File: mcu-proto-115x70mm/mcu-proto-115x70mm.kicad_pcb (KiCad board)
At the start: 2 copper layers, 115 x 70 mm, 1113 parts, among them J1 Conn_01x01

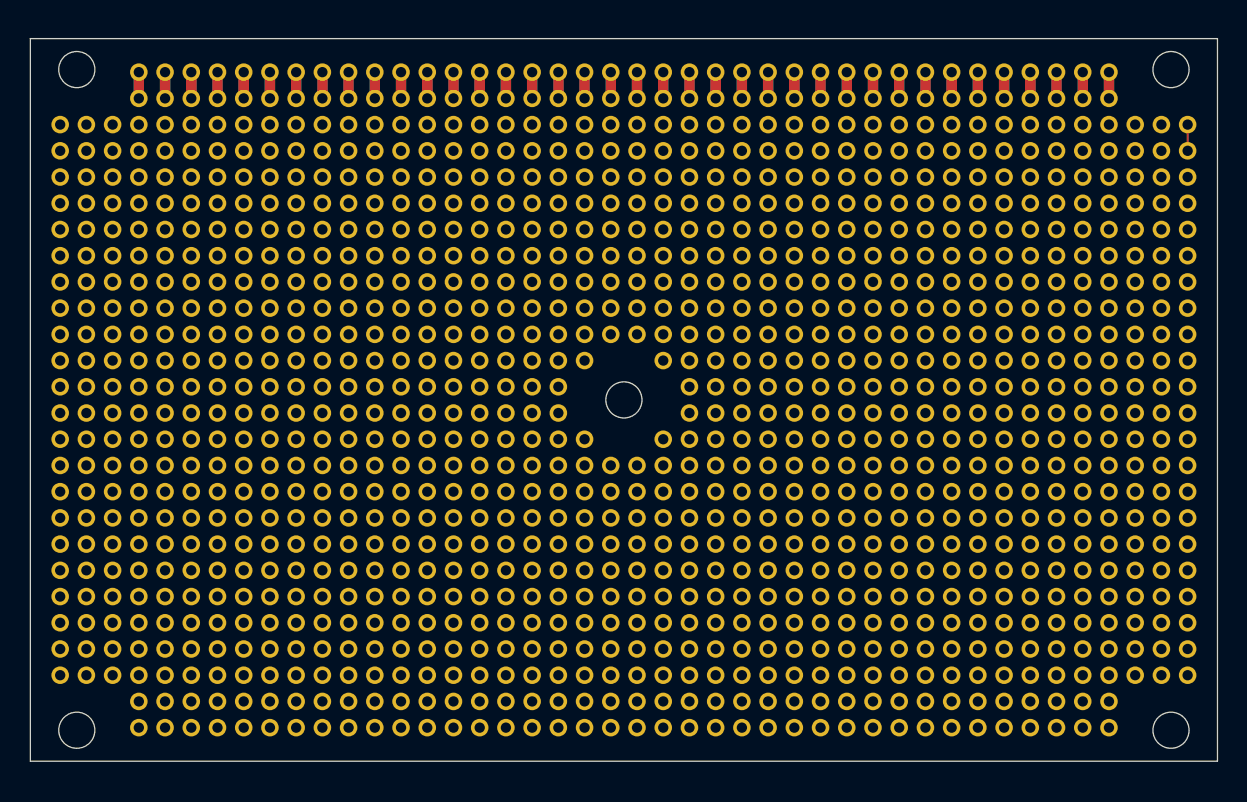
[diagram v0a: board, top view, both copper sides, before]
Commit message: Board routed with mounting holes and silkscreens ready
- Completed PCB routing for mcu-proto-115x70mm
- Added mounting holes for secure enclosure attachment
- Implemented silkscreen layer with component labels and markings
- Generated Gerber files and SVG previews for manufacturing
- Added PadLink footprint for enhanced connectivity
- Updated symbol library and footprint definitions
- Cleaned up old backup files and added new development snapshots
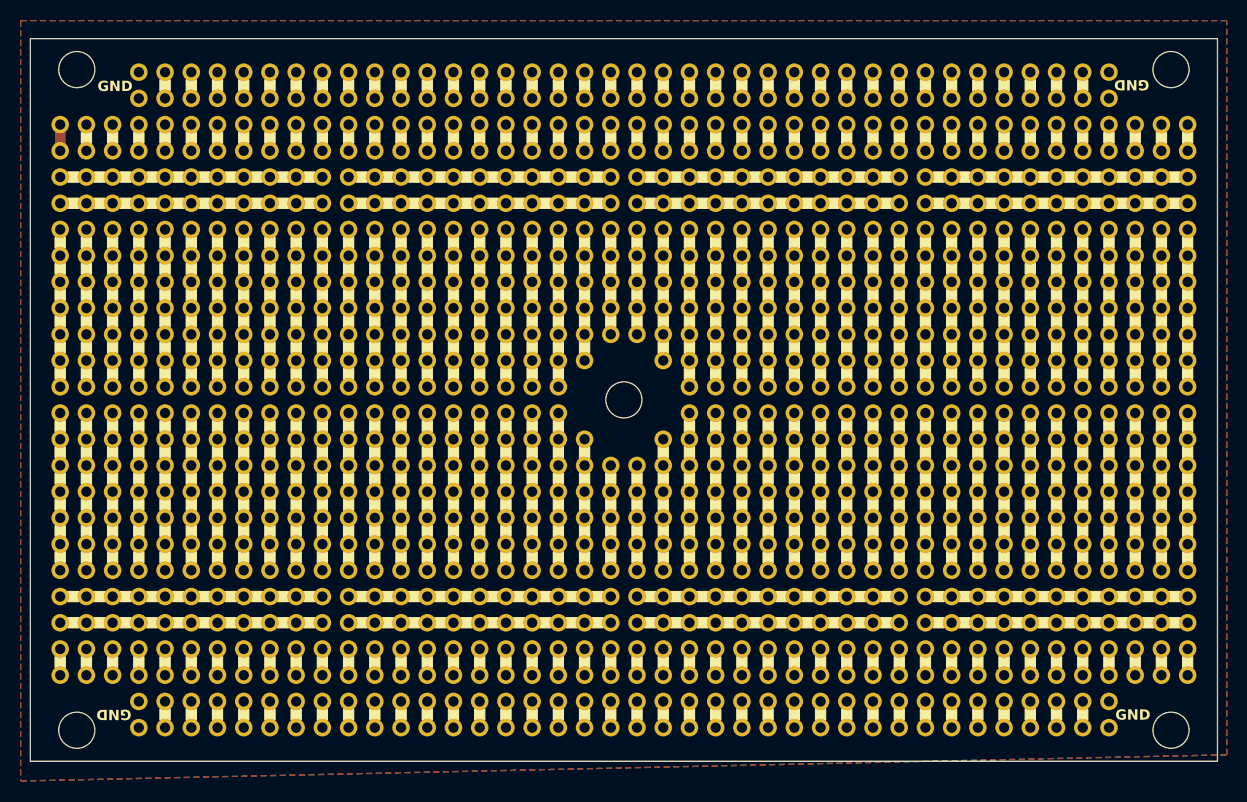
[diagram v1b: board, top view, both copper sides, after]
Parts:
- removed J1 (x1108): Conn_01x01, proto-pcb-pads:RoundPad_1.7mm_Hole_1.0mm
- added REF**: Round_Pad_1.7mm_Hole_1.0mm, proto-pcb-pads:RoundPad_1.7mm_Hole_1.0mm, F.Cu at (110.5, 53.2)
- added REF**: Pad_Link_1.7mm_Width_1.0mm, proto-pcb-silks:PadLink_1.7mm_Width_1.0mm, F.Cu at (113.0, 53.2)
- added REF**: Round_Pad_1.7mm_Hole_1.0mm, proto-pcb-pads:RoundPad_1.7mm_Hole_1.0mm, F.Cu at (113.0, 53.2)
- added REF**1: Round_Pad_1.7mm_Hole_1.0mm, proto-pcb-pads:RoundPad_1.7mm_Hole_1.0mm, F.Cu at (115.6, 53.2)
- added REF**10: Round_Pad_1.7mm_Hole_1.0mm, proto-pcb-pads:RoundPad_1.7mm_Hole_1.0mm, F.Cu at (138.4, 53.2)
- added REF**100: Round_Pad_1.7mm_Hole_1.0mm, proto-pcb-pads:RoundPad_1.7mm_Hole_1.0mm, F.Cu at (163.8, 58.3)
- added REF**1000: Round_Pad_1.7mm_Hole_1.0mm, proto-pcb-pads:RoundPad_1.7mm_Hole_1.0mm, F.Cu at (102.9, 111.7)
- added REF**1001: Round_Pad_1.7mm_Hole_1.0mm, proto-pcb-pads:RoundPad_1.7mm_Hole_1.0mm, F.Cu at (105.4, 111.7)
- added REF**1002: Round_Pad_1.7mm_Hole_1.0mm, proto-pcb-pads:RoundPad_1.7mm_Hole_1.0mm, F.Cu at (108.0, 111.7)
- added REF**1003: Round_Pad_1.7mm_Hole_1.0mm, proto-pcb-pads:RoundPad_1.7mm_Hole_1.0mm, F.Cu at (110.5, 111.7)
- added REF**1004: Round_Pad_1.7mm_Hole_1.0mm, proto-pcb-pads:RoundPad_1.7mm_Hole_1.0mm, F.Cu at (113.0, 111.7)
- added REF**1005: Round_Pad_1.7mm_Hole_1.0mm, proto-pcb-pads:RoundPad_1.7mm_Hole_1.0mm, F.Cu at (115.6, 111.7)
- added REF**1006: Round_Pad_1.7mm_Hole_1.0mm, proto-pcb-pads:RoundPad_1.7mm_Hole_1.0mm, F.Cu at (118.1, 111.7)
- added REF**1007: Round_Pad_1.7mm_Hole_1.0mm, proto-pcb-pads:RoundPad_1.7mm_Hole_1.0mm, F.Cu at (120.7, 111.7)
- added REF**1008: Round_Pad_1.7mm_Hole_1.0mm, proto-pcb-pads:RoundPad_1.7mm_Hole_1.0mm, F.Cu at (123.2, 111.7)
- added REF**1009: Round_Pad_1.7mm_Hole_1.0mm, proto-pcb-pads:RoundPad_1.7mm_Hole_1.0mm, F.Cu at (125.8, 111.7)
- added REF**101: Round_Pad_1.7mm_Hole_1.0mm, proto-pcb-pads:RoundPad_1.7mm_Hole_1.0mm, F.Cu at (166.4, 58.3)
- added REF**1010: Round_Pad_1.7mm_Hole_1.0mm, proto-pcb-pads:RoundPad_1.7mm_Hole_1.0mm, F.Cu at (128.3, 111.7)
- added REF**1011: Round_Pad_1.7mm_Hole_1.0mm, proto-pcb-pads:RoundPad_1.7mm_Hole_1.0mm, F.Cu at (130.8, 111.7)
- added REF**1012: Round_Pad_1.7mm_Hole_1.0mm, proto-pcb-pads:RoundPad_1.7mm_Hole_1.0mm, F.Cu at (133.4, 111.7)
- added REF**1013: Round_Pad_1.7mm_Hole_1.0mm, proto-pcb-pads:RoundPad_1.7mm_Hole_1.0mm, F.Cu at (135.9, 111.7)
- added REF**1014: Round_Pad_1.7mm_Hole_1.0mm, proto-pcb-pads:RoundPad_1.7mm_Hole_1.0mm, F.Cu at (138.4, 111.7)
- added REF**1015: Round_Pad_1.7mm_Hole_1.0mm, proto-pcb-pads:RoundPad_1.7mm_Hole_1.0mm, F.Cu at (141.0, 111.7)
- added REF**1016: Round_Pad_1.7mm_Hole_1.0mm, proto-pcb-pads:RoundPad_1.7mm_Hole_1.0mm, F.Cu at (143.5, 111.7)
- added REF**1017: Round_Pad_1.7mm_Hole_1.0mm, proto-pcb-pads:RoundPad_1.7mm_Hole_1.0mm, F.Cu at (146.1, 111.7)
- added REF**1018: Round_Pad_1.7mm_Hole_1.0mm, proto-pcb-pads:RoundPad_1.7mm_Hole_1.0mm, F.Cu at (148.6, 111.7)
- added REF**1019: Round_Pad_1.7mm_Hole_1.0mm, proto-pcb-pads:RoundPad_1.7mm_Hole_1.0mm, F.Cu at (151.2, 111.7)
- added REF**102: Round_Pad_1.7mm_Hole_1.0mm, proto-pcb-pads:RoundPad_1.7mm_Hole_1.0mm, F.Cu at (168.9, 58.3)
- added REF**1020: Round_Pad_1.7mm_Hole_1.0mm, proto-pcb-pads:RoundPad_1.7mm_Hole_1.0mm, F.Cu at (153.7, 111.7)
- added REF**1021: Round_Pad_1.7mm_Hole_1.0mm, proto-pcb-pads:RoundPad_1.7mm_Hole_1.0mm, F.Cu at (156.2, 111.7)
- added REF**1022: Round_Pad_1.7mm_Hole_1.0mm, proto-pcb-pads:RoundPad_1.7mm_Hole_1.0mm, F.Cu at (158.8, 111.7)
- added REF**1023: Round_Pad_1.7mm_Hole_1.0mm, proto-pcb-pads:RoundPad_1.7mm_Hole_1.0mm, F.Cu at (161.3, 111.7)
- added REF**1024: Round_Pad_1.7mm_Hole_1.0mm, proto-pcb-pads:RoundPad_1.7mm_Hole_1.0mm, F.Cu at (163.8, 111.7)
- added REF**1025: Round_Pad_1.7mm_Hole_1.0mm, proto-pcb-pads:RoundPad_1.7mm_Hole_1.0mm, F.Cu at (166.4, 111.7)
- added REF**1026: Round_Pad_1.7mm_Hole_1.0mm, proto-pcb-pads:RoundPad_1.7mm_Hole_1.0mm, F.Cu at (168.9, 111.7)
- added REF**1027: Round_Pad_1.7mm_Hole_1.0mm, proto-pcb-pads:RoundPad_1.7mm_Hole_1.0mm, F.Cu at (171.5, 111.7)
- added REF**1028: Round_Pad_1.7mm_Hole_1.0mm, proto-pcb-pads:RoundPad_1.7mm_Hole_1.0mm, F.Cu at (174.0, 111.7)
- added REF**1029: Round_Pad_1.7mm_Hole_1.0mm, proto-pcb-pads:RoundPad_1.7mm_Hole_1.0mm, F.Cu at (176.6, 111.7)
- added REF**103: Round_Pad_1.7mm_Hole_1.0mm, proto-pcb-pads:RoundPad_1.7mm_Hole_1.0mm, F.Cu at (171.5, 58.3)
- added REF**1030: Round_Pad_1.7mm_Hole_1.0mm, proto-pcb-pads:RoundPad_1.7mm_Hole_1.0mm, F.Cu at (179.1, 111.7)
- added REF**1031: Round_Pad_1.7mm_Hole_1.0mm, proto-pcb-pads:RoundPad_1.7mm_Hole_1.0mm, F.Cu at (181.6, 111.7)
- added REF**1032: Round_Pad_1.7mm_Hole_1.0mm, proto-pcb-pads:RoundPad_1.7mm_Hole_1.0mm, F.Cu at (184.2, 111.7)
- added REF**1033: Round_Pad_1.7mm_Hole_1.0mm, proto-pcb-pads:RoundPad_1.7mm_Hole_1.0mm, F.Cu at (186.7, 111.7)
- added REF**1034: Round_Pad_1.7mm_Hole_1.0mm, proto-pcb-pads:RoundPad_1.7mm_Hole_1.0mm, F.Cu at (189.2, 111.7)
- added REF**1035: Round_Pad_1.7mm_Hole_1.0mm, proto-pcb-pads:RoundPad_1.7mm_Hole_1.0mm, F.Cu at (191.8, 111.7)
- added REF**1036: Round_Pad_1.7mm_Hole_1.0mm, proto-pcb-pads:RoundPad_1.7mm_Hole_1.0mm, F.Cu at (194.3, 111.7)
- added REF**1037: Round_Pad_1.7mm_Hole_1.0mm, proto-pcb-pads:RoundPad_1.7mm_Hole_1.0mm, F.Cu at (196.9, 111.7)
- added REF**1038: Round_Pad_1.7mm_Hole_1.0mm, proto-pcb-pads:RoundPad_1.7mm_Hole_1.0mm, F.Cu at (199.4, 111.7)
- added REF**1039: Round_Pad_1.7mm_Hole_1.0mm, proto-pcb-pads:RoundPad_1.7mm_Hole_1.0mm, F.Cu at (201.9, 111.7)
- added REF**104: Round_Pad_1.7mm_Hole_1.0mm, proto-pcb-pads:RoundPad_1.7mm_Hole_1.0mm, F.Cu at (174.0, 58.3)
- added REF**1040: Round_Pad_1.7mm_Hole_1.0mm, proto-pcb-pads:RoundPad_1.7mm_Hole_1.0mm, F.Cu at (204.5, 111.7)
- added REF**1041: Round_Pad_1.7mm_Hole_1.0mm, proto-pcb-pads:RoundPad_1.7mm_Hole_1.0mm, F.Cu at (207.0, 111.7)
- added REF**1042: Round_Pad_1.7mm_Hole_1.0mm, proto-pcb-pads:RoundPad_1.7mm_Hole_1.0mm, F.Cu at (209.6, 111.7)
- added REF**1043: Round_Pad_1.7mm_Hole_1.0mm, proto-pcb-pads:RoundPad_1.7mm_Hole_1.0mm, F.Cu at (212.1, 111.7)
- added REF**1044: Pad_Link_1.7mm_Width_1.0mm, proto-pcb-silks:PadLink_1.7mm_Width_1.0mm, F.Cu at (148.6, 53.2)
- added REF**1045: Pad_Link_1.7mm_Width_1.0mm, proto-pcb-silks:PadLink_1.7mm_Width_1.0mm, F.Cu at (151.2, 53.2)
- added REF**1046: Pad_Link_1.7mm_Width_1.0mm, proto-pcb-silks:PadLink_1.7mm_Width_1.0mm, F.Cu at (153.7, 53.2)
- added REF**1047: Round_Pad_1.7mm_Hole_1.0mm, proto-pcb-pads:RoundPad_1.7mm_Hole_1.0mm, F.Cu at (110.5, 114.2)
- added REF**1048: Round_Pad_1.7mm_Hole_1.0mm, proto-pcb-pads:RoundPad_1.7mm_Hole_1.0mm, F.Cu at (113.0, 114.2)
- added REF**1049: Round_Pad_1.7mm_Hole_1.0mm, proto-pcb-pads:RoundPad_1.7mm_Hole_1.0mm, F.Cu at (115.6, 114.2)
- added REF**105: Round_Pad_1.7mm_Hole_1.0mm, proto-pcb-pads:RoundPad_1.7mm_Hole_1.0mm, F.Cu at (176.6, 58.3)
- added REF**1050: Round_Pad_1.7mm_Hole_1.0mm, proto-pcb-pads:RoundPad_1.7mm_Hole_1.0mm, F.Cu at (118.1, 114.2)
- added REF**1051: Round_Pad_1.7mm_Hole_1.0mm, proto-pcb-pads:RoundPad_1.7mm_Hole_1.0mm, F.Cu at (120.7, 114.2)
- added REF**1052: Round_Pad_1.7mm_Hole_1.0mm, proto-pcb-pads:RoundPad_1.7mm_Hole_1.0mm, F.Cu at (123.2, 114.2)
- added REF**1053: Round_Pad_1.7mm_Hole_1.0mm, proto-pcb-pads:RoundPad_1.7mm_Hole_1.0mm, F.Cu at (125.8, 114.2)
- added REF**1054: Round_Pad_1.7mm_Hole_1.0mm, proto-pcb-pads:RoundPad_1.7mm_Hole_1.0mm, F.Cu at (128.3, 114.2)
- added REF**1055: Round_Pad_1.7mm_Hole_1.0mm, proto-pcb-pads:RoundPad_1.7mm_Hole_1.0mm, F.Cu at (130.8, 114.2)
- added REF**1056: Round_Pad_1.7mm_Hole_1.0mm, proto-pcb-pads:RoundPad_1.7mm_Hole_1.0mm, F.Cu at (133.4, 114.2)
- added REF**1057: Round_Pad_1.7mm_Hole_1.0mm, proto-pcb-pads:RoundPad_1.7mm_Hole_1.0mm, F.Cu at (135.9, 114.2)
- added REF**1058: Round_Pad_1.7mm_Hole_1.0mm, proto-pcb-pads:RoundPad_1.7mm_Hole_1.0mm, F.Cu at (138.4, 114.2)
- added REF**1059: Round_Pad_1.7mm_Hole_1.0mm, proto-pcb-pads:RoundPad_1.7mm_Hole_1.0mm, F.Cu at (141.0, 114.2)
- added REF**106: Round_Pad_1.7mm_Hole_1.0mm, proto-pcb-pads:RoundPad_1.7mm_Hole_1.0mm, F.Cu at (179.1, 58.3)
- added REF**1060: Round_Pad_1.7mm_Hole_1.0mm, proto-pcb-pads:RoundPad_1.7mm_Hole_1.0mm, F.Cu at (143.5, 114.2)
- added REF**1061: Round_Pad_1.7mm_Hole_1.0mm, proto-pcb-pads:RoundPad_1.7mm_Hole_1.0mm, F.Cu at (146.1, 114.2)
- added REF**1062: Round_Pad_1.7mm_Hole_1.0mm, proto-pcb-pads:RoundPad_1.7mm_Hole_1.0mm, F.Cu at (148.6, 114.2)
- added REF**1063: Round_Pad_1.7mm_Hole_1.0mm, proto-pcb-pads:RoundPad_1.7mm_Hole_1.0mm, F.Cu at (151.2, 114.2)
- added REF**1064: Round_Pad_1.7mm_Hole_1.0mm, proto-pcb-pads:RoundPad_1.7mm_Hole_1.0mm, F.Cu at (153.7, 114.2)
- added REF**1065: Round_Pad_1.7mm_Hole_1.0mm, proto-pcb-pads:RoundPad_1.7mm_Hole_1.0mm, F.Cu at (156.2, 114.2)
- added REF**1066: Round_Pad_1.7mm_Hole_1.0mm, proto-pcb-pads:RoundPad_1.7mm_Hole_1.0mm, F.Cu at (158.8, 114.2)
- added REF**1067: Round_Pad_1.7mm_Hole_1.0mm, proto-pcb-pads:RoundPad_1.7mm_Hole_1.0mm, F.Cu at (161.3, 114.2)
- added REF**1068: Round_Pad_1.7mm_Hole_1.0mm, proto-pcb-pads:RoundPad_1.7mm_Hole_1.0mm, F.Cu at (163.8, 114.2)
- added REF**1069: Round_Pad_1.7mm_Hole_1.0mm, proto-pcb-pads:RoundPad_1.7mm_Hole_1.0mm, F.Cu at (166.4, 114.2)
- added REF**107: Round_Pad_1.7mm_Hole_1.0mm, proto-pcb-pads:RoundPad_1.7mm_Hole_1.0mm, F.Cu at (181.6, 58.3)
- added REF**1070: Round_Pad_1.7mm_Hole_1.0mm, proto-pcb-pads:RoundPad_1.7mm_Hole_1.0mm, F.Cu at (168.9, 114.2)
- added REF**1071: Round_Pad_1.7mm_Hole_1.0mm, proto-pcb-pads:RoundPad_1.7mm_Hole_1.0mm, F.Cu at (171.5, 114.2)
- added REF**1072: Round_Pad_1.7mm_Hole_1.0mm, proto-pcb-pads:RoundPad_1.7mm_Hole_1.0mm, F.Cu at (174.0, 114.2)
- added REF**1073: Round_Pad_1.7mm_Hole_1.0mm, proto-pcb-pads:RoundPad_1.7mm_Hole_1.0mm, F.Cu at (176.6, 114.2)
- added REF**1074: Round_Pad_1.7mm_Hole_1.0mm, proto-pcb-pads:RoundPad_1.7mm_Hole_1.0mm, F.Cu at (179.1, 114.2)
- added REF**1075: Round_Pad_1.7mm_Hole_1.0mm, proto-pcb-pads:RoundPad_1.7mm_Hole_1.0mm, F.Cu at (181.6, 114.2)
- added REF**1076: Round_Pad_1.7mm_Hole_1.0mm, proto-pcb-pads:RoundPad_1.7mm_Hole_1.0mm, F.Cu at (184.2, 114.2)
- added REF**1077: Round_Pad_1.7mm_Hole_1.0mm, proto-pcb-pads:RoundPad_1.7mm_Hole_1.0mm, F.Cu at (186.7, 114.2)
- added REF**1078: Round_Pad_1.7mm_Hole_1.0mm, proto-pcb-pads:RoundPad_1.7mm_Hole_1.0mm, F.Cu at (189.2, 114.2)
- added REF**1079: Round_Pad_1.7mm_Hole_1.0mm, proto-pcb-pads:RoundPad_1.7mm_Hole_1.0mm, F.Cu at (191.8, 114.2)
- added REF**108: Round_Pad_1.7mm_Hole_1.0mm, proto-pcb-pads:RoundPad_1.7mm_Hole_1.0mm, F.Cu at (184.2, 58.3)
- added REF**1080: Round_Pad_1.7mm_Hole_1.0mm, proto-pcb-pads:RoundPad_1.7mm_Hole_1.0mm, F.Cu at (194.3, 114.2)
- added REF**1081: Round_Pad_1.7mm_Hole_1.0mm, proto-pcb-pads:RoundPad_1.7mm_Hole_1.0mm, F.Cu at (196.9, 114.2)
- added REF**1082: Round_Pad_1.7mm_Hole_1.0mm, proto-pcb-pads:RoundPad_1.7mm_Hole_1.0mm, F.Cu at (199.4, 114.2)
- added REF**1083: Round_Pad_1.7mm_Hole_1.0mm, proto-pcb-pads:RoundPad_1.7mm_Hole_1.0mm, F.Cu at (201.9, 114.2)
- added REF**1084: Round_Pad_1.7mm_Hole_1.0mm, proto-pcb-pads:RoundPad_1.7mm_Hole_1.0mm, F.Cu at (204.5, 114.2)
- added REF**1085: Pad_Link_1.7mm_Width_1.0mm, proto-pcb-silks:PadLink_1.7mm_Width_1.0mm, F.Cu at (156.2, 53.2)
- added REF**1086: Pad_Link_1.7mm_Width_1.0mm, proto-pcb-silks:PadLink_1.7mm_Width_1.0mm, F.Cu at (158.8, 53.2)
- added REF**1087: Pad_Link_1.7mm_Width_1.0mm, proto-pcb-silks:PadLink_1.7mm_Width_1.0mm, F.Cu at (161.3, 53.2)
- added REF**1088: Pad_Link_1.7mm_Width_1.0mm, proto-pcb-silks:PadLink_1.7mm_Width_1.0mm, F.Cu at (163.8, 53.2)
- added REF**1089: Pad_Link_1.7mm_Width_1.0mm, proto-pcb-silks:PadLink_1.7mm_Width_1.0mm, F.Cu at (166.4, 53.2)
- added REF**109: Round_Pad_1.7mm_Hole_1.0mm, proto-pcb-pads:RoundPad_1.7mm_Hole_1.0mm, F.Cu at (186.7, 58.3)
- added REF**1090: Pad_Link_1.7mm_Width_1.0mm, proto-pcb-silks:PadLink_1.7mm_Width_1.0mm, F.Cu at (168.9, 53.2)
- added REF**1091: Round_Pad_1.7mm_Hole_1.0mm, proto-pcb-pads:RoundPad_1.7mm_Hole_1.0mm, F.Cu at (110.5, 116.8)
- added REF**1092: Round_Pad_1.7mm_Hole_1.0mm, proto-pcb-pads:RoundPad_1.7mm_Hole_1.0mm, F.Cu at (113.0, 116.8)
- added REF**1093: Round_Pad_1.7mm_Hole_1.0mm, proto-pcb-pads:RoundPad_1.7mm_Hole_1.0mm, F.Cu at (115.6, 116.8)
- added REF**1094: Round_Pad_1.7mm_Hole_1.0mm, proto-pcb-pads:RoundPad_1.7mm_Hole_1.0mm, F.Cu at (118.1, 116.8)
- added REF**1095: Round_Pad_1.7mm_Hole_1.0mm, proto-pcb-pads:RoundPad_1.7mm_Hole_1.0mm, F.Cu at (120.7, 116.8)
- added REF**1096: Round_Pad_1.7mm_Hole_1.0mm, proto-pcb-pads:RoundPad_1.7mm_Hole_1.0mm, F.Cu at (123.2, 116.8)
- added REF**1097: Round_Pad_1.7mm_Hole_1.0mm, proto-pcb-pads:RoundPad_1.7mm_Hole_1.0mm, F.Cu at (125.8, 116.8)
- added REF**1098: Round_Pad_1.7mm_Hole_1.0mm, proto-pcb-pads:RoundPad_1.7mm_Hole_1.0mm, F.Cu at (128.3, 116.8)
- added REF**1099: Round_Pad_1.7mm_Hole_1.0mm, proto-pcb-pads:RoundPad_1.7mm_Hole_1.0mm, F.Cu at (130.8, 116.8)
- added REF**11: Round_Pad_1.7mm_Hole_1.0mm, proto-pcb-pads:RoundPad_1.7mm_Hole_1.0mm, F.Cu at (141.0, 53.2)
- added REF**110: Round_Pad_1.7mm_Hole_1.0mm, proto-pcb-pads:RoundPad_1.7mm_Hole_1.0mm, F.Cu at (189.2, 58.3)
- added REF**1100: Round_Pad_1.7mm_Hole_1.0mm, proto-pcb-pads:RoundPad_1.7mm_Hole_1.0mm, F.Cu at (133.4, 116.8)
- added REF**1101: Round_Pad_1.7mm_Hole_1.0mm, proto-pcb-pads:RoundPad_1.7mm_Hole_1.0mm, F.Cu at (135.9, 116.8)
- added REF**1102: Round_Pad_1.7mm_Hole_1.0mm, proto-pcb-pads:RoundPad_1.7mm_Hole_1.0mm, F.Cu at (138.4, 116.8)
- added REF**1103: Round_Pad_1.7mm_Hole_1.0mm, proto-pcb-pads:RoundPad_1.7mm_Hole_1.0mm, F.Cu at (141.0, 116.8)
- added REF**1104: Round_Pad_1.7mm_Hole_1.0mm, proto-pcb-pads:RoundPad_1.7mm_Hole_1.0mm, F.Cu at (143.5, 116.8)
- added REF**1105: Round_Pad_1.7mm_Hole_1.0mm, proto-pcb-pads:RoundPad_1.7mm_Hole_1.0mm, F.Cu at (146.1, 116.8)
- added REF**1106: Round_Pad_1.7mm_Hole_1.0mm, proto-pcb-pads:RoundPad_1.7mm_Hole_1.0mm, F.Cu at (148.6, 116.8)
- added REF**1107: Round_Pad_1.7mm_Hole_1.0mm, proto-pcb-pads:RoundPad_1.7mm_Hole_1.0mm, F.Cu at (151.2, 116.8)
- added REF**1108: Round_Pad_1.7mm_Hole_1.0mm, proto-pcb-pads:RoundPad_1.7mm_Hole_1.0mm, F.Cu at (153.7, 116.8)
- added REF**1109: Round_Pad_1.7mm_Hole_1.0mm, proto-pcb-pads:RoundPad_1.7mm_Hole_1.0mm, F.Cu at (156.2, 116.8)
- added REF**111: Round_Pad_1.7mm_Hole_1.0mm, proto-pcb-pads:RoundPad_1.7mm_Hole_1.0mm, F.Cu at (191.8, 58.3)
- added REF**1110: Round_Pad_1.7mm_Hole_1.0mm, proto-pcb-pads:RoundPad_1.7mm_Hole_1.0mm, F.Cu at (158.8, 116.8)
- added REF**1111: Round_Pad_1.7mm_Hole_1.0mm, proto-pcb-pads:RoundPad_1.7mm_Hole_1.0mm, F.Cu at (161.3, 116.8)
- added REF**1112: Round_Pad_1.7mm_Hole_1.0mm, proto-pcb-pads:RoundPad_1.7mm_Hole_1.0mm, F.Cu at (163.8, 116.8)
- added REF**1113: Round_Pad_1.7mm_Hole_1.0mm, proto-pcb-pads:RoundPad_1.7mm_Hole_1.0mm, F.Cu at (166.4, 116.8)
- added REF**1114: Round_Pad_1.7mm_Hole_1.0mm, proto-pcb-pads:RoundPad_1.7mm_Hole_1.0mm, F.Cu at (168.9, 116.8)
- added REF**1115: Round_Pad_1.7mm_Hole_1.0mm, proto-pcb-pads:RoundPad_1.7mm_Hole_1.0mm, F.Cu at (171.5, 116.8)
- added REF**1116: Round_Pad_1.7mm_Hole_1.0mm, proto-pcb-pads:RoundPad_1.7mm_Hole_1.0mm, F.Cu at (174.0, 116.8)
- added REF**1117: Round_Pad_1.7mm_Hole_1.0mm, proto-pcb-pads:RoundPad_1.7mm_Hole_1.0mm, F.Cu at (176.6, 116.8)
- added REF**1118: Round_Pad_1.7mm_Hole_1.0mm, proto-pcb-pads:RoundPad_1.7mm_Hole_1.0mm, F.Cu at (179.1, 116.8)
- added REF**1119: Round_Pad_1.7mm_Hole_1.0mm, proto-pcb-pads:RoundPad_1.7mm_Hole_1.0mm, F.Cu at (181.6, 116.8)
- added REF**112: Round_Pad_1.7mm_Hole_1.0mm, proto-pcb-pads:RoundPad_1.7mm_Hole_1.0mm, F.Cu at (194.3, 58.3)
- added REF**1120: Round_Pad_1.7mm_Hole_1.0mm, proto-pcb-pads:RoundPad_1.7mm_Hole_1.0mm, F.Cu at (184.2, 116.8)
- added REF**1121: Round_Pad_1.7mm_Hole_1.0mm, proto-pcb-pads:RoundPad_1.7mm_Hole_1.0mm, F.Cu at (186.7, 116.8)
- added REF**1122: Round_Pad_1.7mm_Hole_1.0mm, proto-pcb-pads:RoundPad_1.7mm_Hole_1.0mm, F.Cu at (189.2, 116.8)
- added REF**1123: Round_Pad_1.7mm_Hole_1.0mm, proto-pcb-pads:RoundPad_1.7mm_Hole_1.0mm, F.Cu at (191.8, 116.8)
- added REF**1124: Round_Pad_1.7mm_Hole_1.0mm, proto-pcb-pads:RoundPad_1.7mm_Hole_1.0mm, F.Cu at (194.3, 116.8)
- added REF**1125: Round_Pad_1.7mm_Hole_1.0mm, proto-pcb-pads:RoundPad_1.7mm_Hole_1.0mm, F.Cu at (196.9, 116.8)
- added REF**1126: Round_Pad_1.7mm_Hole_1.0mm, proto-pcb-pads:RoundPad_1.7mm_Hole_1.0mm, F.Cu at (199.4, 116.8)
- added REF**1127: Round_Pad_1.7mm_Hole_1.0mm, proto-pcb-pads:RoundPad_1.7mm_Hole_1.0mm, F.Cu at (201.9, 116.8)
- added REF**1128: Round_Pad_1.7mm_Hole_1.0mm, proto-pcb-pads:RoundPad_1.7mm_Hole_1.0mm, F.Cu at (204.5, 116.8)
- added REF**1129: Pad_Link_1.7mm_Width_1.0mm, proto-pcb-silks:PadLink_1.7mm_Width_1.0mm, F.Cu at (171.5, 53.2)
- added REF**113: Round_Pad_1.7mm_Hole_1.0mm, proto-pcb-pads:RoundPad_1.7mm_Hole_1.0mm, F.Cu at (196.9, 58.3)
- added REF**1130: Pad_Link_1.7mm_Width_1.0mm, proto-pcb-silks:PadLink_1.7mm_Width_1.0mm, F.Cu at (174.0, 53.2)
- added REF**1131: Pad_Link_1.7mm_Width_1.0mm, proto-pcb-silks:PadLink_1.7mm_Width_1.0mm, F.Cu at (176.6, 53.2)
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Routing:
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- added copper zone on B.Cu, net GND
- added copper zone on F.Cu, net GND
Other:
- board text added: "GND"

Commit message: Silkscreen on both sides and descriptive text. Generating gerbers for single board
- Added silkscreen layer on both front and back sides of PCB
- Implemented descriptive text and component labels on both faces
- Generated complete Gerber files for single board manufacturing
- Included copper layers (F_Cu, B_Cu), mask layers (F_Mask, B_Mask)
- Added silkscreen layers (F_Silkscreen, B_Silkscreen) for both sides
- Generated drill files (PTH.drl, NPTH.drl) for hole drilling
- Created edge cuts file for board outline definition
- Packaged all manufacturing files in single.zip for easy distribution
- Updated MCU proto 100x68mm project files
- Cleaned up old backup files and added new development snapshots
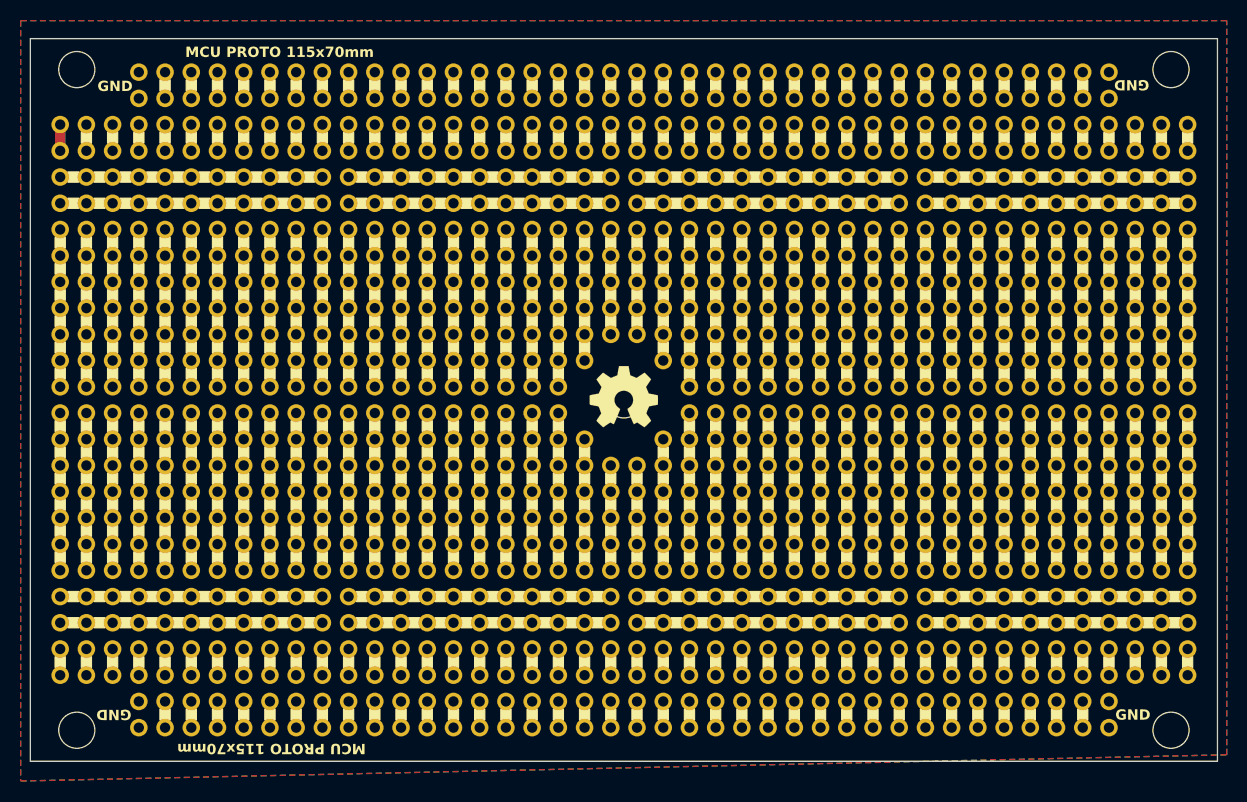
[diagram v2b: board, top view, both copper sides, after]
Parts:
- added REF**: OSHW-Symbol_6.7x6mm_SilkScreen, Symbol:OSHW-Symbol_6.7x6mm_SilkScreen, F.Cu at (157.5, 84.7)
- added REF**: Pad_Link_1.7mm_Width_1.0mm, proto-pcb-silks:PadLink_1.7mm_Width_1.0mm, B.Cu at (113.0, 53.2)
- added REF**: OSHW-Symbol_6.7x6mm_SilkScreen, Symbol:OSHW-Symbol_6.7x6mm_SilkScreen, B.Cu at (157.5, 85.3)
- added REF**1940: Pad_Link_1.7mm_Width_1.0mm, proto-pcb-silks:PadLink_1.7mm_Width_1.0mm, B.Cu at (115.6, 53.2)
- added REF**1941: Pad_Link_1.7mm_Width_1.0mm, proto-pcb-silks:PadLink_1.7mm_Width_1.0mm, B.Cu at (118.1, 53.2)
- added REF**1942: Pad_Link_1.7mm_Width_1.0mm, proto-pcb-silks:PadLink_1.7mm_Width_1.0mm, B.Cu at (120.7, 53.2)
- added REF**1943: Pad_Link_1.7mm_Width_1.0mm, proto-pcb-silks:PadLink_1.7mm_Width_1.0mm, B.Cu at (123.2, 53.2)
- added REF**1944: Pad_Link_1.7mm_Width_1.0mm, proto-pcb-silks:PadLink_1.7mm_Width_1.0mm, B.Cu at (125.8, 53.2)
- added REF**1945: Pad_Link_1.7mm_Width_1.0mm, proto-pcb-silks:PadLink_1.7mm_Width_1.0mm, B.Cu at (128.3, 53.2)
- added REF**1946: Pad_Link_1.7mm_Width_1.0mm, proto-pcb-silks:PadLink_1.7mm_Width_1.0mm, B.Cu at (130.8, 53.2)
- added REF**1947: Pad_Link_1.7mm_Width_1.0mm, proto-pcb-silks:PadLink_1.7mm_Width_1.0mm, B.Cu at (133.4, 53.2)
- added REF**1948: Pad_Link_1.7mm_Width_1.0mm, proto-pcb-silks:PadLink_1.7mm_Width_1.0mm, B.Cu at (135.9, 53.2)
- added REF**1949: Pad_Link_1.7mm_Width_1.0mm, proto-pcb-silks:PadLink_1.7mm_Width_1.0mm, B.Cu at (138.4, 53.2)
- added REF**1950: Pad_Link_1.7mm_Width_1.0mm, proto-pcb-silks:PadLink_1.7mm_Width_1.0mm, B.Cu at (141.0, 53.2)
- added REF**1951: Pad_Link_1.7mm_Width_1.0mm, proto-pcb-silks:PadLink_1.7mm_Width_1.0mm, B.Cu at (143.5, 53.2)
- added REF**1952: Pad_Link_1.7mm_Width_1.0mm, proto-pcb-silks:PadLink_1.7mm_Width_1.0mm, B.Cu at (146.1, 53.2)
- added REF**1953: Pad_Link_1.7mm_Width_1.0mm, proto-pcb-silks:PadLink_1.7mm_Width_1.0mm, B.Cu at (148.6, 53.2)
- added REF**1954: Pad_Link_1.7mm_Width_1.0mm, proto-pcb-silks:PadLink_1.7mm_Width_1.0mm, B.Cu at (151.2, 53.2)
- added REF**1955: Pad_Link_1.7mm_Width_1.0mm, proto-pcb-silks:PadLink_1.7mm_Width_1.0mm, B.Cu at (153.7, 53.2)
- added REF**1956: Pad_Link_1.7mm_Width_1.0mm, proto-pcb-silks:PadLink_1.7mm_Width_1.0mm, B.Cu at (156.2, 53.2)
- added REF**1957: Pad_Link_1.7mm_Width_1.0mm, proto-pcb-silks:PadLink_1.7mm_Width_1.0mm, B.Cu at (158.8, 53.2)
- added REF**1958: Pad_Link_1.7mm_Width_1.0mm, proto-pcb-silks:PadLink_1.7mm_Width_1.0mm, B.Cu at (161.3, 53.2)
- added REF**1959: Pad_Link_1.7mm_Width_1.0mm, proto-pcb-silks:PadLink_1.7mm_Width_1.0mm, B.Cu at (163.8, 53.2)
- added REF**1960: Pad_Link_1.7mm_Width_1.0mm, proto-pcb-silks:PadLink_1.7mm_Width_1.0mm, B.Cu at (166.4, 53.2)
- added REF**1961: Pad_Link_1.7mm_Width_1.0mm, proto-pcb-silks:PadLink_1.7mm_Width_1.0mm, B.Cu at (168.9, 53.2)
- added REF**1962: Pad_Link_1.7mm_Width_1.0mm, proto-pcb-silks:PadLink_1.7mm_Width_1.0mm, B.Cu at (171.5, 53.2)
- added REF**1963: Pad_Link_1.7mm_Width_1.0mm, proto-pcb-silks:PadLink_1.7mm_Width_1.0mm, B.Cu at (174.0, 53.2)
- added REF**1964: Pad_Link_1.7mm_Width_1.0mm, proto-pcb-silks:PadLink_1.7mm_Width_1.0mm, B.Cu at (176.6, 53.2)
- added REF**1965: Pad_Link_1.7mm_Width_1.0mm, proto-pcb-silks:PadLink_1.7mm_Width_1.0mm, B.Cu at (179.1, 53.2)
- added REF**1966: Pad_Link_1.7mm_Width_1.0mm, proto-pcb-silks:PadLink_1.7mm_Width_1.0mm, B.Cu at (181.6, 53.2)
- added REF**1967: Pad_Link_1.7mm_Width_1.0mm, proto-pcb-silks:PadLink_1.7mm_Width_1.0mm, B.Cu at (184.2, 53.2)
- added REF**1968: Pad_Link_1.7mm_Width_1.0mm, proto-pcb-silks:PadLink_1.7mm_Width_1.0mm, B.Cu at (186.7, 53.2)
- added REF**1969: Pad_Link_1.7mm_Width_1.0mm, proto-pcb-silks:PadLink_1.7mm_Width_1.0mm, B.Cu at (189.2, 53.2)
- added REF**1970: Pad_Link_1.7mm_Width_1.0mm, proto-pcb-silks:PadLink_1.7mm_Width_1.0mm, B.Cu at (191.8, 53.2)
- added REF**1971: Pad_Link_1.7mm_Width_1.0mm, proto-pcb-silks:PadLink_1.7mm_Width_1.0mm, B.Cu at (194.3, 53.2)
- added REF**1972: Pad_Link_1.7mm_Width_1.0mm, proto-pcb-silks:PadLink_1.7mm_Width_1.0mm, B.Cu at (196.9, 53.2)
- added REF**1973: Pad_Link_1.7mm_Width_1.0mm, proto-pcb-silks:PadLink_1.7mm_Width_1.0mm, B.Cu at (199.4, 53.2)
- added REF**1974: Pad_Link_1.7mm_Width_1.0mm, proto-pcb-silks:PadLink_1.7mm_Width_1.0mm, B.Cu at (201.9, 53.2)
- added REF**1975: Pad_Link_1.7mm_Width_1.0mm, proto-pcb-silks:PadLink_1.7mm_Width_1.0mm, B.Cu at (102.9, 58.3)
- added REF**1976: Pad_Link_1.7mm_Width_1.0mm, proto-pcb-silks:PadLink_1.7mm_Width_1.0mm, B.Cu at (105.4, 58.3)
- added REF**1977: Pad_Link_1.7mm_Width_1.0mm, proto-pcb-silks:PadLink_1.7mm_Width_1.0mm, B.Cu at (108.0, 58.3)
- added REF**1978: Pad_Link_1.7mm_Width_1.0mm, proto-pcb-silks:PadLink_1.7mm_Width_1.0mm, B.Cu at (110.5, 58.3)
- added REF**1979: Pad_Link_1.7mm_Width_1.0mm, proto-pcb-silks:PadLink_1.7mm_Width_1.0mm, B.Cu at (113.0, 58.3)
- added REF**1980: Pad_Link_1.7mm_Width_1.0mm, proto-pcb-silks:PadLink_1.7mm_Width_1.0mm, B.Cu at (115.6, 58.3)
- added REF**1981: Pad_Link_1.7mm_Width_1.0mm, proto-pcb-silks:PadLink_1.7mm_Width_1.0mm, B.Cu at (118.1, 58.3)
- added REF**1982: Pad_Link_1.7mm_Width_1.0mm, proto-pcb-silks:PadLink_1.7mm_Width_1.0mm, B.Cu at (120.7, 58.3)
- added REF**1983: Pad_Link_1.7mm_Width_1.0mm, proto-pcb-silks:PadLink_1.7mm_Width_1.0mm, B.Cu at (123.2, 58.3)
- added REF**1984: Pad_Link_1.7mm_Width_1.0mm, proto-pcb-silks:PadLink_1.7mm_Width_1.0mm, B.Cu at (125.8, 58.3)
- added REF**1985: Pad_Link_1.7mm_Width_1.0mm, proto-pcb-silks:PadLink_1.7mm_Width_1.0mm, B.Cu at (128.3, 58.3)
- added REF**1986: Pad_Link_1.7mm_Width_1.0mm, proto-pcb-silks:PadLink_1.7mm_Width_1.0mm, B.Cu at (130.8, 58.3)
- added REF**1987: Pad_Link_1.7mm_Width_1.0mm, proto-pcb-silks:PadLink_1.7mm_Width_1.0mm, B.Cu at (133.4, 58.3)
- added REF**1988: Pad_Link_1.7mm_Width_1.0mm, proto-pcb-silks:PadLink_1.7mm_Width_1.0mm, B.Cu at (135.9, 58.3)
- added REF**1989: Pad_Link_1.7mm_Width_1.0mm, proto-pcb-silks:PadLink_1.7mm_Width_1.0mm, B.Cu at (138.4, 58.3)
- added REF**1990: Pad_Link_1.7mm_Width_1.0mm, proto-pcb-silks:PadLink_1.7mm_Width_1.0mm, B.Cu at (141.0, 58.3)
- added REF**1991: Pad_Link_1.7mm_Width_1.0mm, proto-pcb-silks:PadLink_1.7mm_Width_1.0mm, B.Cu at (143.5, 58.3)
- added REF**1992: Pad_Link_1.7mm_Width_1.0mm, proto-pcb-silks:PadLink_1.7mm_Width_1.0mm, B.Cu at (146.1, 58.3)
- added REF**1993: Pad_Link_1.7mm_Width_1.0mm, proto-pcb-silks:PadLink_1.7mm_Width_1.0mm, B.Cu at (148.6, 58.3)
- added REF**1994: Pad_Link_1.7mm_Width_1.0mm, proto-pcb-silks:PadLink_1.7mm_Width_1.0mm, B.Cu at (151.2, 58.3)
- added REF**1995: Pad_Link_1.7mm_Width_1.0mm, proto-pcb-silks:PadLink_1.7mm_Width_1.0mm, B.Cu at (153.7, 58.3)
- added REF**1996: Pad_Link_1.7mm_Width_1.0mm, proto-pcb-silks:PadLink_1.7mm_Width_1.0mm, B.Cu at (156.2, 58.3)
- added REF**1997: Pad_Link_1.7mm_Width_1.0mm, proto-pcb-silks:PadLink_1.7mm_Width_1.0mm, B.Cu at (158.8, 58.3)
- added REF**1998: Pad_Link_1.7mm_Width_1.0mm, proto-pcb-silks:PadLink_1.7mm_Width_1.0mm, B.Cu at (161.3, 58.3)
- added REF**1999: Pad_Link_1.7mm_Width_1.0mm, proto-pcb-silks:PadLink_1.7mm_Width_1.0mm, B.Cu at (163.8, 58.3)
- added REF**2000: Pad_Link_1.7mm_Width_1.0mm, proto-pcb-silks:PadLink_1.7mm_Width_1.0mm, B.Cu at (166.4, 58.3)
- added REF**2001: Pad_Link_1.7mm_Width_1.0mm, proto-pcb-silks:PadLink_1.7mm_Width_1.0mm, B.Cu at (168.9, 58.3)
- added REF**2002: Pad_Link_1.7mm_Width_1.0mm, proto-pcb-silks:PadLink_1.7mm_Width_1.0mm, B.Cu at (171.5, 58.3)
- added REF**2003: Pad_Link_1.7mm_Width_1.0mm, proto-pcb-silks:PadLink_1.7mm_Width_1.0mm, B.Cu at (174.0, 58.3)
- added REF**2004: Pad_Link_1.7mm_Width_1.0mm, proto-pcb-silks:PadLink_1.7mm_Width_1.0mm, B.Cu at (176.6, 58.3)
- added REF**2005: Pad_Link_1.7mm_Width_1.0mm, proto-pcb-silks:PadLink_1.7mm_Width_1.0mm, B.Cu at (179.1, 58.3)
- added REF**2006: Pad_Link_1.7mm_Width_1.0mm, proto-pcb-silks:PadLink_1.7mm_Width_1.0mm, B.Cu at (181.6, 58.3)
- added REF**2007: Pad_Link_1.7mm_Width_1.0mm, proto-pcb-silks:PadLink_1.7mm_Width_1.0mm, B.Cu at (184.2, 58.3)
- added REF**2008: Pad_Link_1.7mm_Width_1.0mm, proto-pcb-silks:PadLink_1.7mm_Width_1.0mm, B.Cu at (186.7, 58.3)
- added REF**2009: Pad_Link_1.7mm_Width_1.0mm, proto-pcb-silks:PadLink_1.7mm_Width_1.0mm, B.Cu at (189.2, 58.3)
- added REF**2010: Pad_Link_1.7mm_Width_1.0mm, proto-pcb-silks:PadLink_1.7mm_Width_1.0mm, B.Cu at (191.8, 58.3)
- added REF**2011: Pad_Link_1.7mm_Width_1.0mm, proto-pcb-silks:PadLink_1.7mm_Width_1.0mm, B.Cu at (194.3, 58.3)
- added REF**2012: Pad_Link_1.7mm_Width_1.0mm, proto-pcb-silks:PadLink_1.7mm_Width_1.0mm, B.Cu at (196.9, 58.3)
- added REF**2013: Pad_Link_1.7mm_Width_1.0mm, proto-pcb-silks:PadLink_1.7mm_Width_1.0mm, B.Cu at (199.4, 58.3)
- added REF**2014: Pad_Link_1.7mm_Width_1.0mm, proto-pcb-silks:PadLink_1.7mm_Width_1.0mm, B.Cu at (201.9, 58.3)
- added REF**2015: Pad_Link_1.7mm_Width_1.0mm, proto-pcb-silks:PadLink_1.7mm_Width_1.0mm, B.Cu at (204.5, 58.3)
- added REF**2016: Pad_Link_1.7mm_Width_1.0mm, proto-pcb-silks:PadLink_1.7mm_Width_1.0mm, B.Cu at (207.0, 58.3)
- added REF**2017: Pad_Link_1.7mm_Width_1.0mm, proto-pcb-silks:PadLink_1.7mm_Width_1.0mm, B.Cu at (209.6, 58.3)
- added REF**2018: Pad_Link_1.7mm_Width_1.0mm, proto-pcb-silks:PadLink_1.7mm_Width_1.0mm, B.Cu at (212.1, 58.3)
- added REF**2019: Pad_Link_1.7mm_Width_1.0mm, proto-pcb-silks:PadLink_1.7mm_Width_1.0mm, B.Cu at (102.9, 63.4)
- added REF**2020: Pad_Link_1.7mm_Width_1.0mm, proto-pcb-silks:PadLink_1.7mm_Width_1.0mm, B.Cu at (102.9, 66.0)
- added REF**2021: Pad_Link_1.7mm_Width_1.0mm, proto-pcb-silks:PadLink_1.7mm_Width_1.0mm, B.Cu at (105.4, 63.4)
- added REF**2022: Pad_Link_1.7mm_Width_1.0mm, proto-pcb-silks:PadLink_1.7mm_Width_1.0mm, B.Cu at (108.0, 63.4)
- added REF**2023: Pad_Link_1.7mm_Width_1.0mm, proto-pcb-silks:PadLink_1.7mm_Width_1.0mm, B.Cu at (110.5, 63.4)
- added REF**2024: Pad_Link_1.7mm_Width_1.0mm, proto-pcb-silks:PadLink_1.7mm_Width_1.0mm, B.Cu at (113.0, 63.4)
- added REF**2025: Pad_Link_1.7mm_Width_1.0mm, proto-pcb-silks:PadLink_1.7mm_Width_1.0mm, B.Cu at (115.6, 63.4)
- added REF**2026: Pad_Link_1.7mm_Width_1.0mm, proto-pcb-silks:PadLink_1.7mm_Width_1.0mm, B.Cu at (118.1, 63.4)
- added REF**2027: Pad_Link_1.7mm_Width_1.0mm, proto-pcb-silks:PadLink_1.7mm_Width_1.0mm, B.Cu at (120.7, 63.4)
- added REF**2028: Pad_Link_1.7mm_Width_1.0mm, proto-pcb-silks:PadLink_1.7mm_Width_1.0mm, B.Cu at (123.2, 63.4)
- added REF**2029: Pad_Link_1.7mm_Width_1.0mm, proto-pcb-silks:PadLink_1.7mm_Width_1.0mm, B.Cu at (125.8, 63.4)
- added REF**2030: Pad_Link_1.7mm_Width_1.0mm, proto-pcb-silks:PadLink_1.7mm_Width_1.0mm, B.Cu at (105.4, 66.0)
- added REF**2031: Pad_Link_1.7mm_Width_1.0mm, proto-pcb-silks:PadLink_1.7mm_Width_1.0mm, B.Cu at (130.8, 63.4)
- added REF**2032: Pad_Link_1.7mm_Width_1.0mm, proto-pcb-silks:PadLink_1.7mm_Width_1.0mm, B.Cu at (133.4, 63.4)
- added REF**2033: Pad_Link_1.7mm_Width_1.0mm, proto-pcb-silks:PadLink_1.7mm_Width_1.0mm, B.Cu at (135.9, 63.4)
- added REF**2034: Pad_Link_1.7mm_Width_1.0mm, proto-pcb-silks:PadLink_1.7mm_Width_1.0mm, B.Cu at (138.4, 63.4)
- added REF**2035: Pad_Link_1.7mm_Width_1.0mm, proto-pcb-silks:PadLink_1.7mm_Width_1.0mm, B.Cu at (141.0, 63.4)
- added REF**2036: Pad_Link_1.7mm_Width_1.0mm, proto-pcb-silks:PadLink_1.7mm_Width_1.0mm, B.Cu at (143.5, 63.4)
- added REF**2037: Pad_Link_1.7mm_Width_1.0mm, proto-pcb-silks:PadLink_1.7mm_Width_1.0mm, B.Cu at (146.1, 63.4)
- added REF**2038: Pad_Link_1.7mm_Width_1.0mm, proto-pcb-silks:PadLink_1.7mm_Width_1.0mm, B.Cu at (148.6, 63.4)
- added REF**2039: Pad_Link_1.7mm_Width_1.0mm, proto-pcb-silks:PadLink_1.7mm_Width_1.0mm, B.Cu at (151.2, 63.4)
- added REF**2040: Pad_Link_1.7mm_Width_1.0mm, proto-pcb-silks:PadLink_1.7mm_Width_1.0mm, B.Cu at (153.7, 63.4)
- added REF**2041: Pad_Link_1.7mm_Width_1.0mm, proto-pcb-silks:PadLink_1.7mm_Width_1.0mm, B.Cu at (108.0, 66.0)
- added REF**2042: Pad_Link_1.7mm_Width_1.0mm, proto-pcb-silks:PadLink_1.7mm_Width_1.0mm, B.Cu at (158.8, 63.4)
- added REF**2043: Pad_Link_1.7mm_Width_1.0mm, proto-pcb-silks:PadLink_1.7mm_Width_1.0mm, B.Cu at (161.3, 63.4)
- added REF**2044: Pad_Link_1.7mm_Width_1.0mm, proto-pcb-silks:PadLink_1.7mm_Width_1.0mm, B.Cu at (163.8, 63.4)
- added REF**2045: Pad_Link_1.7mm_Width_1.0mm, proto-pcb-silks:PadLink_1.7mm_Width_1.0mm, B.Cu at (166.4, 63.4)
- added REF**2046: Pad_Link_1.7mm_Width_1.0mm, proto-pcb-silks:PadLink_1.7mm_Width_1.0mm, B.Cu at (168.9, 63.4)
- added REF**2047: Pad_Link_1.7mm_Width_1.0mm, proto-pcb-silks:PadLink_1.7mm_Width_1.0mm, B.Cu at (171.5, 63.4)
- added REF**2048: Pad_Link_1.7mm_Width_1.0mm, proto-pcb-silks:PadLink_1.7mm_Width_1.0mm, B.Cu at (174.0, 63.4)
- added REF**2049: Pad_Link_1.7mm_Width_1.0mm, proto-pcb-silks:PadLink_1.7mm_Width_1.0mm, B.Cu at (176.6, 63.4)
- added REF**2050: Pad_Link_1.7mm_Width_1.0mm, proto-pcb-silks:PadLink_1.7mm_Width_1.0mm, B.Cu at (179.1, 63.4)
- added REF**2051: Pad_Link_1.7mm_Width_1.0mm, proto-pcb-silks:PadLink_1.7mm_Width_1.0mm, B.Cu at (181.6, 63.4)
- added REF**2052: Pad_Link_1.7mm_Width_1.0mm, proto-pcb-silks:PadLink_1.7mm_Width_1.0mm, B.Cu at (110.5, 66.0)
- added REF**2053: Pad_Link_1.7mm_Width_1.0mm, proto-pcb-silks:PadLink_1.7mm_Width_1.0mm, B.Cu at (186.7, 63.4)
- added REF**2054: Pad_Link_1.7mm_Width_1.0mm, proto-pcb-silks:PadLink_1.7mm_Width_1.0mm, B.Cu at (189.2, 63.4)
- added REF**2055: Pad_Link_1.7mm_Width_1.0mm, proto-pcb-silks:PadLink_1.7mm_Width_1.0mm, B.Cu at (191.8, 63.4)
- added REF**2056: Pad_Link_1.7mm_Width_1.0mm, proto-pcb-silks:PadLink_1.7mm_Width_1.0mm, B.Cu at (194.3, 63.4)
- added REF**2057: Pad_Link_1.7mm_Width_1.0mm, proto-pcb-silks:PadLink_1.7mm_Width_1.0mm, B.Cu at (196.9, 63.4)
- added REF**2058: Pad_Link_1.7mm_Width_1.0mm, proto-pcb-silks:PadLink_1.7mm_Width_1.0mm, B.Cu at (199.4, 63.4)
- added REF**2059: Pad_Link_1.7mm_Width_1.0mm, proto-pcb-silks:PadLink_1.7mm_Width_1.0mm, B.Cu at (201.9, 63.4)
- added REF**2060: Pad_Link_1.7mm_Width_1.0mm, proto-pcb-silks:PadLink_1.7mm_Width_1.0mm, B.Cu at (204.5, 63.4)
- added REF**2061: Pad_Link_1.7mm_Width_1.0mm, proto-pcb-silks:PadLink_1.7mm_Width_1.0mm, B.Cu at (207.0, 63.4)
- added REF**2062: Pad_Link_1.7mm_Width_1.0mm, proto-pcb-silks:PadLink_1.7mm_Width_1.0mm, B.Cu at (209.6, 63.4)
- added REF**2063: Pad_Link_1.7mm_Width_1.0mm, proto-pcb-silks:PadLink_1.7mm_Width_1.0mm, B.Cu at (113.0, 66.0)
- added REF**2064: Pad_Link_1.7mm_Width_1.0mm, proto-pcb-silks:PadLink_1.7mm_Width_1.0mm, B.Cu at (115.6, 66.0)
- added REF**2065: Pad_Link_1.7mm_Width_1.0mm, proto-pcb-silks:PadLink_1.7mm_Width_1.0mm, B.Cu at (118.1, 66.0)
- added REF**2066: Pad_Link_1.7mm_Width_1.0mm, proto-pcb-silks:PadLink_1.7mm_Width_1.0mm, B.Cu at (120.7, 66.0)
- added REF**2067: Pad_Link_1.7mm_Width_1.0mm, proto-pcb-silks:PadLink_1.7mm_Width_1.0mm, B.Cu at (123.2, 66.0)
- added REF**2068: Pad_Link_1.7mm_Width_1.0mm, proto-pcb-silks:PadLink_1.7mm_Width_1.0mm, B.Cu at (125.8, 66.0)
- added REF**2069: Pad_Link_1.7mm_Width_1.0mm, proto-pcb-silks:PadLink_1.7mm_Width_1.0mm, B.Cu at (102.9, 109.1)
- added REF**2070: Pad_Link_1.7mm_Width_1.0mm, proto-pcb-silks:PadLink_1.7mm_Width_1.0mm, B.Cu at (130.8, 66.0)
- added REF**2071: Pad_Link_1.7mm_Width_1.0mm, proto-pcb-silks:PadLink_1.7mm_Width_1.0mm, B.Cu at (133.4, 66.0)
- added REF**2072: Pad_Link_1.7mm_Width_1.0mm, proto-pcb-silks:PadLink_1.7mm_Width_1.0mm, B.Cu at (135.9, 66.0)
- added REF**2073: Pad_Link_1.7mm_Width_1.0mm, proto-pcb-silks:PadLink_1.7mm_Width_1.0mm, B.Cu at (138.4, 66.0)
- added REF**2074: Pad_Link_1.7mm_Width_1.0mm, proto-pcb-silks:PadLink_1.7mm_Width_1.0mm, B.Cu at (141.0, 66.0)
- added REF**2075: Pad_Link_1.7mm_Width_1.0mm, proto-pcb-silks:PadLink_1.7mm_Width_1.0mm, B.Cu at (143.5, 66.0)
- added REF**2076: Pad_Link_1.7mm_Width_1.0mm, proto-pcb-silks:PadLink_1.7mm_Width_1.0mm, B.Cu at (146.1, 66.0)
- added REF**2077: Pad_Link_1.7mm_Width_1.0mm, proto-pcb-silks:PadLink_1.7mm_Width_1.0mm, B.Cu at (148.6, 66.0)
- added REF**2078: Pad_Link_1.7mm_Width_1.0mm, proto-pcb-silks:PadLink_1.7mm_Width_1.0mm, B.Cu at (151.2, 66.0)
- added REF**2079: Pad_Link_1.7mm_Width_1.0mm, proto-pcb-silks:PadLink_1.7mm_Width_1.0mm, B.Cu at (153.7, 66.0)
- added REF**2080: Pad_Link_1.7mm_Width_1.0mm, proto-pcb-silks:PadLink_1.7mm_Width_1.0mm, B.Cu at (113.0, 114.2)
- added REF**2081: Pad_Link_1.7mm_Width_1.0mm, proto-pcb-silks:PadLink_1.7mm_Width_1.0mm, B.Cu at (158.8, 66.0)
- added REF**2082: Pad_Link_1.7mm_Width_1.0mm, proto-pcb-silks:PadLink_1.7mm_Width_1.0mm, B.Cu at (161.3, 66.0)
- added REF**2083: Pad_Link_1.7mm_Width_1.0mm, proto-pcb-silks:PadLink_1.7mm_Width_1.0mm, B.Cu at (163.8, 66.0)
- added REF**2084: Pad_Link_1.7mm_Width_1.0mm, proto-pcb-silks:PadLink_1.7mm_Width_1.0mm, B.Cu at (166.4, 66.0)
- added REF**2085: Pad_Link_1.7mm_Width_1.0mm, proto-pcb-silks:PadLink_1.7mm_Width_1.0mm, B.Cu at (168.9, 66.0)
- added REF**2086: Pad_Link_1.7mm_Width_1.0mm, proto-pcb-silks:PadLink_1.7mm_Width_1.0mm, B.Cu at (171.5, 66.0)
- added REF**2087: Pad_Link_1.7mm_Width_1.0mm, proto-pcb-silks:PadLink_1.7mm_Width_1.0mm, B.Cu at (174.0, 66.0)
- added REF**2088: Pad_Link_1.7mm_Width_1.0mm, proto-pcb-silks:PadLink_1.7mm_Width_1.0mm, B.Cu at (176.6, 66.0)
- added REF**2089: Pad_Link_1.7mm_Width_1.0mm, proto-pcb-silks:PadLink_1.7mm_Width_1.0mm, B.Cu at (179.1, 66.0)
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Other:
- board text added: "MCU PROTO 115x70mm"
